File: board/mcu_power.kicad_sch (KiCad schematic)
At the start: 8 parts

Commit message: initial board layout (WIP), schematic tuning
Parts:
- C16, C19: LCSC C115671 -> C307331
- C17: LCSC C274416 -> C23733
- C18: LCSC C314234 -> C52923
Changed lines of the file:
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@@
       (effects (font (size 1.27 1.27)) hide)
     )
-    (property "LCSC" "C115671" (at 81.28 46.99 0)
+    (property "LCSC" "C307331" (at 81.28 46.99 0)
       (effects (font (size 1.27 1.27)) hide)
     )
@@
       (effects (font (size 1.27 1.27)) hide)
     )
+    (pin "1")
     (pin "2")
-    (pin "1")
     (instances
       (project "eprom5vread"
@@
       (effects (font (size 1.27 1.27)) hide)
     )
+    (pin "1")
     (pin "2")
-    (pin "1")
     (instances
       (project "eprom5vread"
@@
       (effects (font (size 1.27 1.27)) hide)
     )
-    (property "LCSC" "C115671" (at 81.28 97.79 0)
+    (property "LCSC" "C307331" (at 81.28 97.79 0)
       (effects (font (size 1.27 1.27)) hide)
     )
@@
       (effects (font (size 1.27 1.27)) hide)
     )
-    (property "LCSC" "C274416" (at 60.96 46.99 0)
+    (property "LCSC" "C23733" (at 60.96 46.99 0)
       (effects (font (size 1.27 1.27)) hide)
     )
@@
       (effects (font (size 1.27 1.27)) hide)
     )
-    (property "LCSC" "C314234" (at 81.28 72.39 0)
+    (property "LCSC" "C52923" (at 81.28 72.39 0)
       (effects (font (size 1.27 1.27)) hide)
     )
@@
       (effects (font (size 1.27 1.27)) hide)
     )
+    (pin "1")
     (pin "2")
-    (pin "1")
     (instances
       (project "eprom5vread"

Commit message: finish board design
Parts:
- renumbered C17 to C101, C16 to C102, C18 to C103, C19 to C104, FB1 to FB101, NT1 to NT101, NT2 to NT102, NT3 to NT103
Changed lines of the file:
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@@
   (junction (at 81.28 40.64) (diameter 0) (color 0 0 0 0)
   )
+  (junction (at 71.12 40.64) (diameter 0) (color 0 0 0 0)
+  )
+  (junction (at 71.12 66.04) (diameter 0) (color 0 0 0 0)
+  )
   (junction (at 60.96 40.64) (diameter 0) (color 0 0 0 0)
   )
@@
     (stroke (width 0) (type default))
   )
-  (wire (pts (xy 81.28 40.64) (xy 60.96 40.64))
+  (wire (pts (xy 81.28 40.64) (xy 71.12 40.64))
     (stroke (width 0) (type default))
   )
@@
     (stroke (width 0) (type default))
   )
+  (wire (pts (xy 71.12 66.04) (xy 81.28 66.04))
+    (stroke (width 0) (type default))
+  )
   (wire (pts (xy 50.8 40.64) (xy 53.34 40.64))
     (stroke (width 0) (type default))
@@
     (stroke (width 0) (type default))
   )
+  (wire (pts (xy 71.12 40.64) (xy 60.96 40.64))
+    (stroke (width 0) (type default))
+  )
   (wire (pts (xy 81.28 93.98) (xy 81.28 91.44))
     (stroke (width 0) (type default))
@@
     (stroke (width 0) (type default))
   )
+  (wire (pts (xy 71.12 63.5) (xy 71.12 66.04))
+    (stroke (width 0) (type default))
+  )
   (wire (pts (xy 81.28 40.64) (xy 81.28 43.18))
     (stroke (width 0) (type default))
@@
     (stroke (width 0) (type default))
   )
+  (wire (pts (xy 71.12 38.1) (xy 71.12 40.64))
+    (stroke (width 0) (type default))
+  )
   (wire (pts (xy 50.8 116.84) (xy 96.52 116.84))
     (stroke (width 0) (type default))
@@
     (stroke (width 0) (type default))
   )
-  (wire (pts (xy 58.42 66.04) (xy 81.28 66.04))
+  (wire (pts (xy 58.42 66.04) (xy 71.12 66.04))
     (stroke (width 0) (type default))
   )
@@
     (effects (font (size 1.27 1.27)) (justify right bottom))
   )
-  (label "VSS" (at 96.52 116.84 180) (fields_autoplaced)
+  (label "GND" (at 96.52 116.84 180) (fields_autoplaced)
     (effects (font (size 1.27 1.27)) (justify right bottom))
   )
@@
   (symbol (lib_id "Device:C") (at 81.28 46.99 0) (unit 1)
     (in_bom yes) (on_board yes) (dnp no) (fields_autoplaced)
-    (property "Reference" "C16" (at 85.09 45.72 0)
+    (property "Reference" "C102" (at 85.09 45.72 0)
       (effects (font (size 1.27 1.27)) (justify left))
     )
@@
       (project "eprom5vread"
         (path "/b08a8275-42d3-43c1-b04c-f89506e7527b/2fd5d481-fecc-449f-aabd-88adee8fd543/8c29ad67-2ca5-4386-bc0e-0233a83181ef"
-          (reference "C16") (unit 1)
+          (reference "C102") (unit 1)
         )
       )
@@
   (symbol (lib_id "Device:NetTie_2") (at 55.88 66.04 0) (unit 1)
     (in_bom no) (on_board yes) (dnp no)
-    (property "Reference" "NT2" (at 55.88 60.96 0)
+    (property "Reference" "NT102" (at 55.88 60.96 0)
       (effects (font (size 1.27 1.27)))
     )
@@
       (project "eprom5vread"
         (path "/b08a8275-42d3-43c1-b04c-f89506e7527b/2fd5d481-fecc-449f-aabd-88adee8fd543/8c29ad67-2ca5-4386-bc0e-0233a83181ef"
-          (reference "NT2") (unit 1)
+          (reference "NT102") (unit 1)
         )
       )
@@
   (symbol (lib_id "Device:FerriteBead") (at 68.58 91.44 90) (unit 1)
     (in_bom yes) (on_board yes) (dnp no)
-    (property "Reference" "FB1" (at 68.58 96.52 90)
+    (property "Reference" "FB101" (at 68.58 96.52 90)
       (effects (font (size 1.27 1.27)))
     )
@@
       (project "eprom5vread"
         (path "/b08a8275-42d3-43c1-b04c-f89506e7527b/2fd5d481-fecc-449f-aabd-88adee8fd543/8c29ad67-2ca5-4386-bc0e-0233a83181ef"
-          (reference "FB1") (unit 1)
+          (reference "FB101") (unit 1)
         )
       )
@@
   (symbol (lib_id "Device:NetTie_2") (at 55.88 40.64 0) (unit 1)
     (in_bom no) (on_board yes) (dnp no)
-    (property "Reference" "NT1" (at 55.88 35.56 0)
+    (property "Reference" "NT101" (at 55.88 35.56 0)
       (effects (font (size 1.27 1.27)))
     )
@@
       (project "eprom5vread"
         (path "/b08a8275-42d3-43c1-b04c-f89506e7527b/2fd5d481-fecc-449f-aabd-88adee8fd543/8c29ad67-2ca5-4386-bc0e-0233a83181ef"
-          (reference "NT1") (unit 1)
+          (reference "NT101") (unit 1)
         )
       )
@@
   (symbol (lib_id "Device:C") (at 81.28 97.79 0) (unit 1)
     (in_bom yes) (on_board yes) (dnp no) (fields_autoplaced)
-    (property "Reference" "C19" (at 85.09 96.52 0)
+    (property "Reference" "C104" (at 85.09 96.52 0)
       (effects (font (size 1.27 1.27)) (justify left))
     )
@@
       (project "eprom5vread"
         (path "/b08a8275-42d3-43c1-b04c-f89506e7527b/2fd5d481-fecc-449f-aabd-88adee8fd543/8c29ad67-2ca5-4386-bc0e-0233a83181ef"
-          (reference "C19") (unit 1)
+          (reference "C104") (unit 1)
         )
       )
@@
   (symbol (lib_id "Device:C") (at 60.96 46.99 0) (unit 1)
     (in_bom yes) (on_board yes) (dnp no) (fields_autoplaced)
-    (property "Reference" "C17" (at 64.77 45.72 0)
+    (property "Reference" "C101" (at 64.77 45.72 0)
       (effects (font (size 1.27 1.27)) (justify left))
     )
@@
       (project "eprom5vread"
         (path "/b08a8275-42d3-43c1-b04c-f89506e7527b/2fd5d481-fecc-449f-aabd-88adee8fd543/8c29ad67-2ca5-4386-bc0e-0233a83181ef"
-          (reference "C17") (unit 1)
+          (reference "C101") (unit 1)
         )
       )
@@
   (symbol (lib_id "Device:C") (at 81.28 72.39 0) (unit 1)
     (in_bom yes) (on_board yes) (dnp no) (fields_autoplaced)
-    (property "Reference" "C18" (at 85.09 71.12 0)
+    (property "Reference" "C103" (at 85.09 71.12 0)
       (effects (font (size 1.27 1.27)) (justify left))
     )
@@
       (project "eprom5vread"
         (path "/b08a8275-42d3-43c1-b04c-f89506e7527b/2fd5d481-fecc-449f-aabd-88adee8fd543/8c29ad67-2ca5-4386-bc0e-0233a83181ef"
-          (reference "C18") (unit 1)
+          (reference "C103") (unit 1)
+        )
+      )
+    )
+  )
+  (symbol (lib_id "power:PWR_FLAG") (at 71.12 63.5 0) (unit 1)
+    (in_bom yes) (on_board yes) (dnp no) (fields_autoplaced)
+    (property "Reference" "#FLG05" (at 71.12 61.595 0)
+      (effects (font (size 1.27 1.27)) hide)
+    )
+    (property "Value" "PWR_FLAG" (at 71.12 58.42 0)
+      (effects (font (size 1.27 1.27)))
+    )
+    (property "Footprint" "" (at 71.12 63.5 0)
+      (effects (font (size 1.27 1.27)) hide)
+    )
+    (property "Datasheet" "~" (at 71.12 63.5 0)
+      (effects (font (size 1.27 1.27)) hide)
+    )
+    (pin "1")
+    (instances
+      (project "eprom5vread"
+        (path "/b08a8275-42d3-43c1-b04c-f89506e7527b/2fd5d481-fecc-449f-aabd-88adee8fd543/8c29ad67-2ca5-4386-bc0e-0233a83181ef"
+          (reference "#FLG05") (unit 1)
         )
       )
@@
   (symbol (lib_id "Device:NetTie_2") (at 55.88 91.44 0) (unit 1)
     (in_bom no) (on_board yes) (dnp no)
-    (property "Reference" "NT3" (at 55.88 86.36 0)
+    (property "Reference" "NT103" (at 55.88 86.36 0)
       (effects (font (size 1.27 1.27)))
     )
@@
       (project "eprom5vread"
         (path "/b08a8275-42d3-43c1-b04c-f89506e7527b/2fd5d481-fecc-449f-aabd-88adee8fd543/8c29ad67-2ca5-4386-bc0e-0233a83181ef"
-          (reference "NT3") (unit 1)
-        )
-      )
+          (reference "NT103") (unit 1)
+        )
+      )
+    )
+  )
+  (symbol (lib_id "power:PWR_FLAG") (at 71.12 38.1 0) (unit 1)
+    (in_bom yes) (on_board yes) (dnp no) (fields_autoplaced)
+    (property "Reference" "#FLG04" (at 71.12 36.195 0)
+      (effects (font (size 1.27 1.27)) hide)
+    )
+    (property "Value" "PWR_FLAG" (at 71.12 33.02 0)
+      (effects (font (size 1.27 1.27)))
+    )
+    (property "Footprint" "" (at 71.12 38.1 0)
+      (effects (font (size 1.27 1.27)) hide)
+    )
+    (property "Datasheet" "~" (at 71.12 38.1 0)
+      (effects (font (size 1.27 1.27)) hide)
+    )
+    (pin "1")
+    (instances
+      (project "eprom5vread"
+        (path "/b08a8275-42d3-43c1-b04c-f89506e7527b/2fd5d481-fecc-449f-aabd-88adee8fd543/8c29ad67-2ca5-4386-bc0e-0233a83181ef"
+          (reference "#FLG04") (unit 1)
+        )
+      )

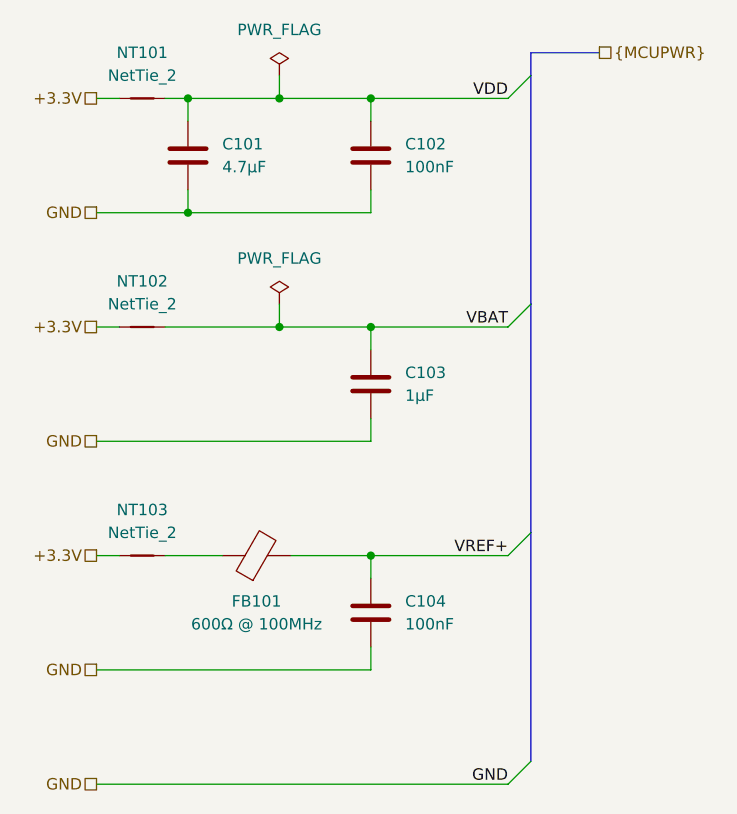
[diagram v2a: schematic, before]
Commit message: redo board to use I2C port expanders (and smaller MCU)
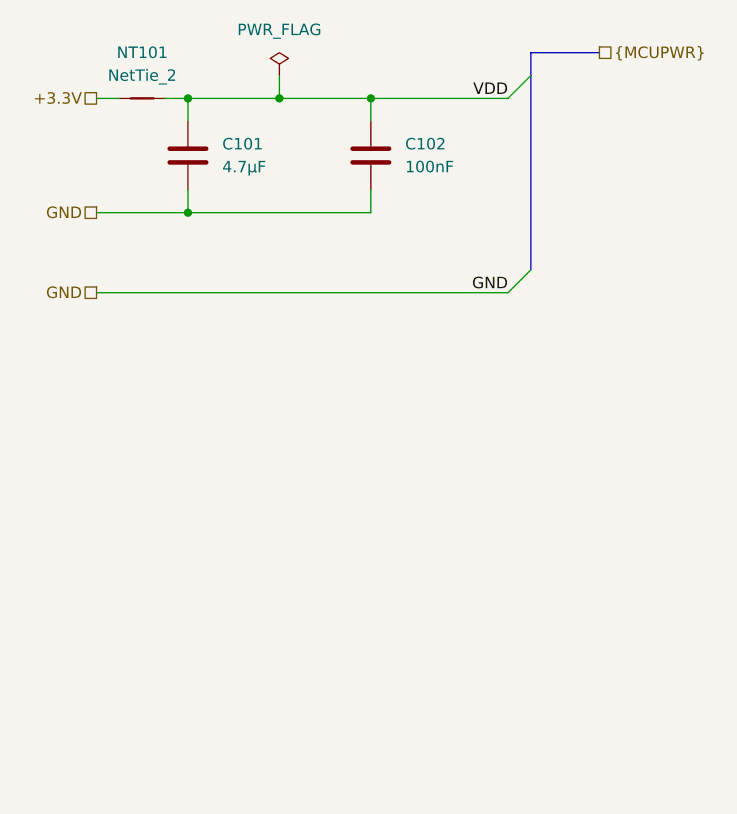
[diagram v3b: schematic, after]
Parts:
- removed C103: 1µF, Capacitor_SMD:C_0402_1005Metric, symbol Device:C
- removed C104: 100nF, Capacitor_SMD:C_0402_1005Metric, symbol Device:C
- removed FB101: 600Ω @ 100MHz, Inductor_SMD:L_0402_1005Metric, symbol Device:FerriteBead
- removed NT102, NT103: NetTie_2, NetTie:NetTie-2_SMD_Pad0.5mm, symbol Device:NetTie_2
